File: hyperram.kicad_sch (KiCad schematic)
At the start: 7 parts, among them U2001 S27KL0641DABHI023

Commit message: Bump revision to 1.0.0
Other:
- title: LPDDR5 Test Board -> SO-DIMM DDR5 Tester

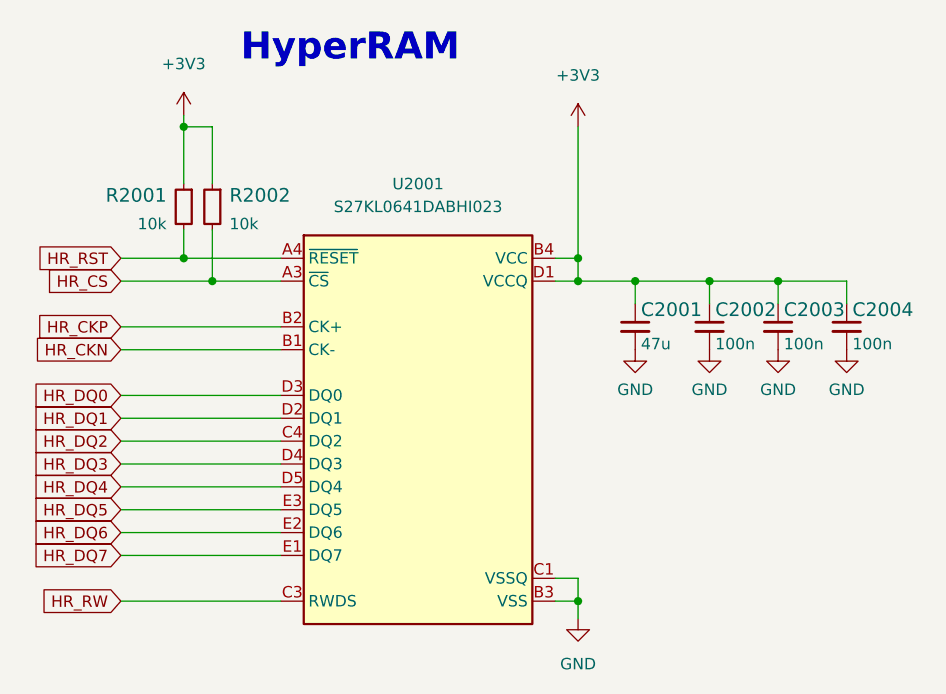
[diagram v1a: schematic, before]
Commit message: Optimize BOM, replace obsolete parts, improve manufacturing attributes
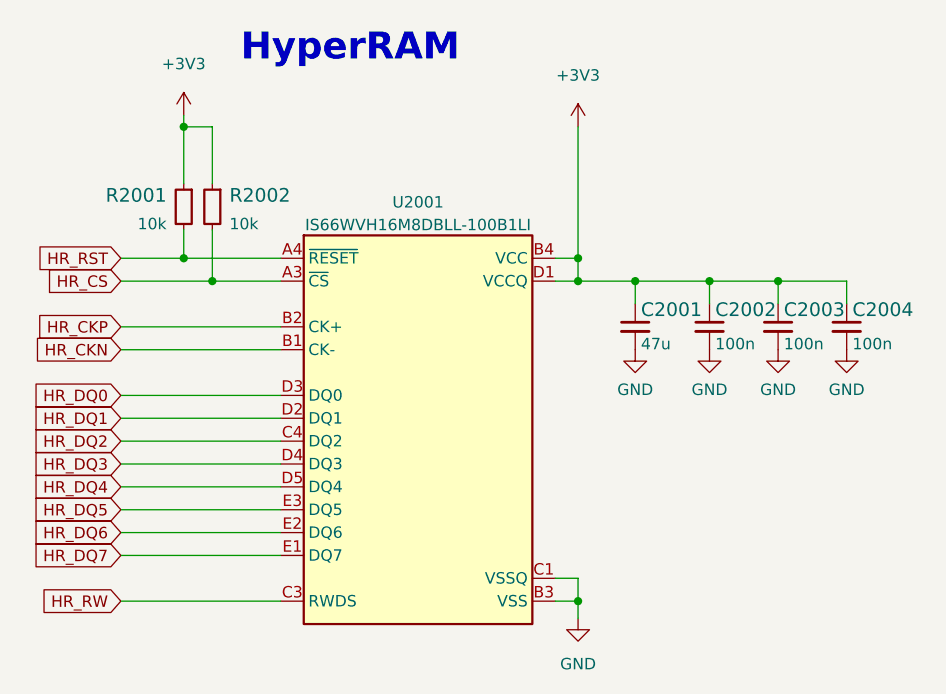
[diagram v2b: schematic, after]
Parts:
- removed U2001: S27KL0641DABHI023, sodimm-ddr5-tester-footprints:FBGA-24-1_6x8mm_Layout5x5_P1mm, symbol sodimm-ddr5-tester:S27KL0641DABHI023
- added U2001: IS66WVH16M8DBLL-100B1LI, antmicro-footprints:FBGA-25-24_6x8mm_Layout5x5_P1mm, symbol antmicroMemory:IS66WVH16M8DBLL-100B1LI
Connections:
- net +3V3: now also U2001.B4 (VCC), U2001.D1 (VCCQ), U2001.E4 (VCCQ)
- net GND: now also U2001.B3 (VSS), U2001.C1 (VSSQ), U2001.E5 (VSSQ)
- net HR_CKN: now also U2001.B1 (CK-)
- net HR_CKP: now also U2001.B2 (CK+)
- net HR_CS: now also U2001.A3 (~{CS})
- net HR_DQ0: now also U2001.D3 (DQ0)
- net HR_DQ1: now also U2001.D2 (DQ1)
- net HR_DQ2: now also U2001.C4 (DQ2)
- net HR_DQ3: now also U2001.D4 (DQ3)
- net HR_DQ4: now also U2001.D5 (DQ4)
- net HR_DQ5: now also U2001.E3 (DQ5)
- net HR_DQ6: now also U2001.E2 (DQ6)
- net HR_DQ7: now also U2001.E1 (DQ7)
- net HR_RST: now also U2001.A4 (~{RESET})
- net HR_RW: now also U2001.C3 (RWDS)
- new net: U2001.A2 (NC), U2001.A5 (NC), U2001.B5 (NC), U2001.C2 (NC), U2001.C5 (NC)
